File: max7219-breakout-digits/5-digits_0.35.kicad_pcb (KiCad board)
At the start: 2 copper layers, 53.5 x 15.5 mm, 6 parts, among them J1 Conn_02x08_Odd_Even, U1 HDSM-443B_7-Segment_2_Digit, U2 HDSM-443B_7-Segment_3_Digit

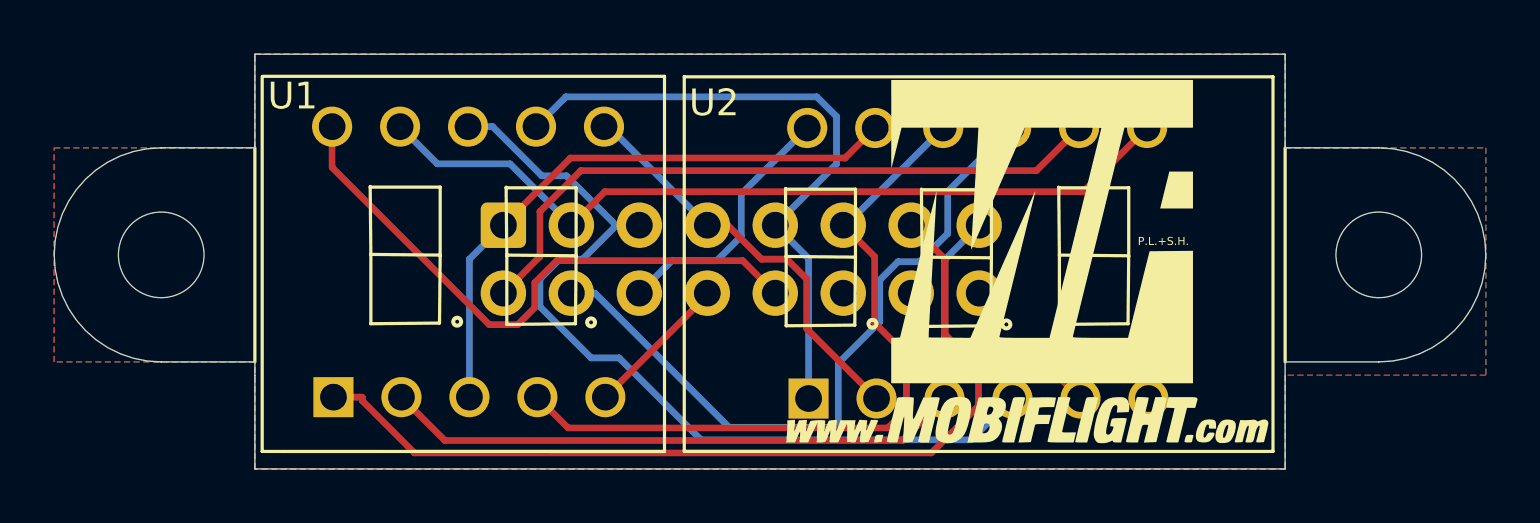
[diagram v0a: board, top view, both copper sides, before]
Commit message: rotate IDC on 0.28 displays, plated mounting holes for 0.35 displays, set version for 0.35 displays
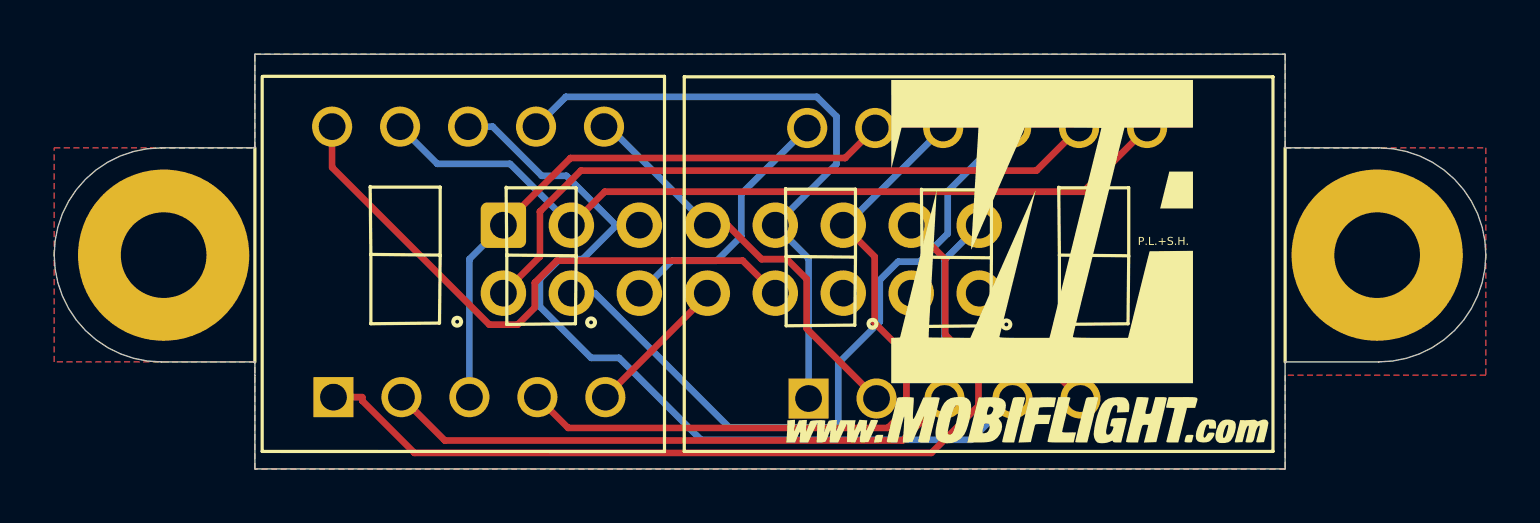
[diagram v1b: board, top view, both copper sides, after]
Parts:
- removed REF1, REF2: MountingHole_3.2mm_M3, MountingHole:MountingHole_3.2mm_M3
- added H1: MountingHole 3.2mm, MountingHole:MountingHole_3.2mm_M3_Pad, F.Cu at (86.6, 47.5)
- added H2: MountingHole 3.2mm, MountingHole:MountingHole_3.2mm_M3_Pad, F.Cu at (131.9, 47.5)
- U1: footprint Display_7Segment:SN42056STH -> MobiFlight:STH_7_2 Digits_0.35_CC
- U2: footprint Display_7Segment:SP42056STH -> MobiFlight:STH_7_3 Digits_0.35_CC
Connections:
- J1 pad 12: (no net) -> unconnected-(J1-Pin_12-Pad12)
- J1 pad 14: (no net) -> unconnected-(J1-Pin_14-Pad14)
- J1 pad 16: (no net) -> unconnected-(J1-Pin_16-Pad16)
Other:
- board text added: "5 Digit Module ${REVISION}"
- board text removed: "5 Digit Module V1.0"
